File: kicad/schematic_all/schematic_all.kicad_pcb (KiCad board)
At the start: 2 copper layers, 88.9 x 88.9 mm, 36 parts, among them J1 Power In, SW1 Button 1, SW2 Encoder 1, SW3 Button 2, SW4 Encoder 2, SW5 Button 3, U2 RPi_Pico, U3 RDA5807M_Module, U4 LM386

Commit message: schematic v0.2
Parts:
- removed C1, C2, C3: 100uF, Capacitor_THT:CP_Radial_D5.0mm_P2.00mm
- removed C11: 10uF, Capacitor_THT:CP_Radial_D5.0mm_P2.00mm
- removed C7: 220nF, Capacitor_THT:CP_Radial_D5.0mm_P2.00mm
- removed C8: 47pF, Capacitor_THT:C_Rect_L7.0mm_W2.5mm_P5.00mm
- removed C9: 22uF, Capacitor_THT:CP_Radial_D5.0mm_P2.00mm
- moved J1 63.0 mm to (125.8, 120.7), turned to 0 degrees
- moved C4 22.5 mm to (64.2, 110.5), turned to 180 degrees
- moved U4 16.2 mm to (108.0, 102.3)
- moved R3 15.5 mm to (69.8, 116.8), turned to 90 degrees
- moved RV1 13.2 mm to (131.4, 56.6)
- moved RV2 13.1 mm to (131.4, 71.8)
- moved C13 12.0 mm to (127.0, 96.5)
- moved R4 11.5 mm to (119.4, 69.8), turned to -90 degrees
- moved LS1 9.60 mm to (139.1, 110.5)
- moved C5 8.91 mm to (127.0, 71.1), turned to 180 degrees
- moved DISP1 8.89 mm to (89.4, 120.7)
- moved C12 7.20 mm to (128.3, 104.1), turned to -90 degrees
- moved C10 6.82 mm to (120.7, 106.1), turned to 90 degrees
- moved R5 5.75 mm to (129.5, 111.8), turned to 180 degrees
- moved C6 3.12 mm to (127.0, 78.7)
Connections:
- R4 pad 1: Net-(C7-Pad1) -> Net-(U4-+)
- RV1 pad 2: Net-(C7-Pad1) -> Net-(U4-+)
- RV1 pad 3: Net-(C7-Pad1) -> Net-(U4-+)
- RV2 pad 2: Net-(C7-Pad1) -> Net-(U4-+)
- RV2 pad 3: Net-(C7-Pad1) -> Net-(U4-+)
- U4 pad 2: Net-(U4--) -> GND
- U4 pad 7: Net-(U4-BYPASS) -> unconnected-(U4-BYPASS-Pad7)
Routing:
- net /SDC: track 60.8 -> 0.00 mm
- net /SCS: track 53.6 -> 0.00 mm
- net /SRES: track 38.5 -> 0.00 mm
- net /SSDA: track 31.4 -> 0.00 mm
- net /SSCK: track 26.8 -> 0.00 mm
- net /ENC2_CL: track 17.5 -> 0.00 mm
- net /ENC2_DR: track 15.7 -> 0.00 mm
- net /ENC2_PB: track 14.7 -> 0.00 mm
- net Net-(AE1-A): track 0.00 -> 14.2 mm
- net /BTN3: track 13.0 -> 0.00 mm
- net /BTN2: track 12.5 -> 0.00 mm

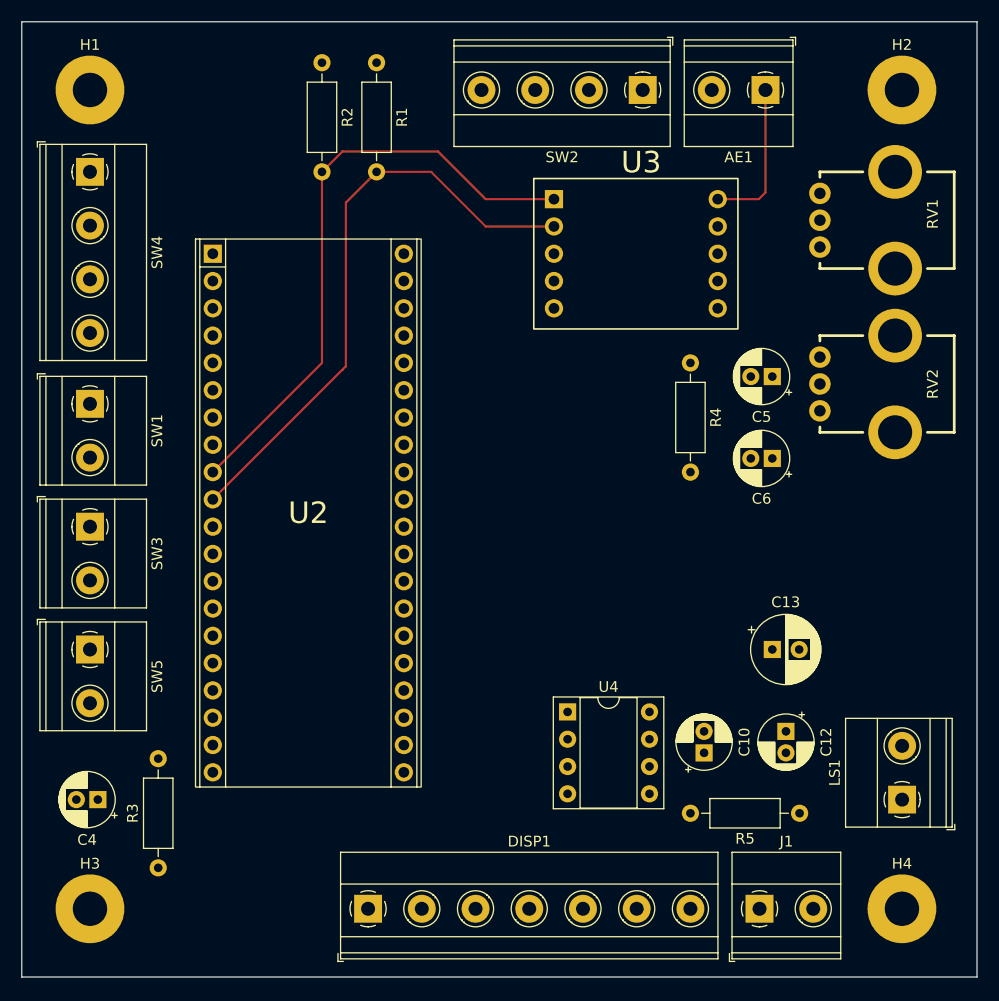
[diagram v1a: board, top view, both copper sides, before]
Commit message: Made some minor changes to the schmatic (Changed PWM pin, filtering capacitor footprints and values), and made some progress on the layout & design of the PCB
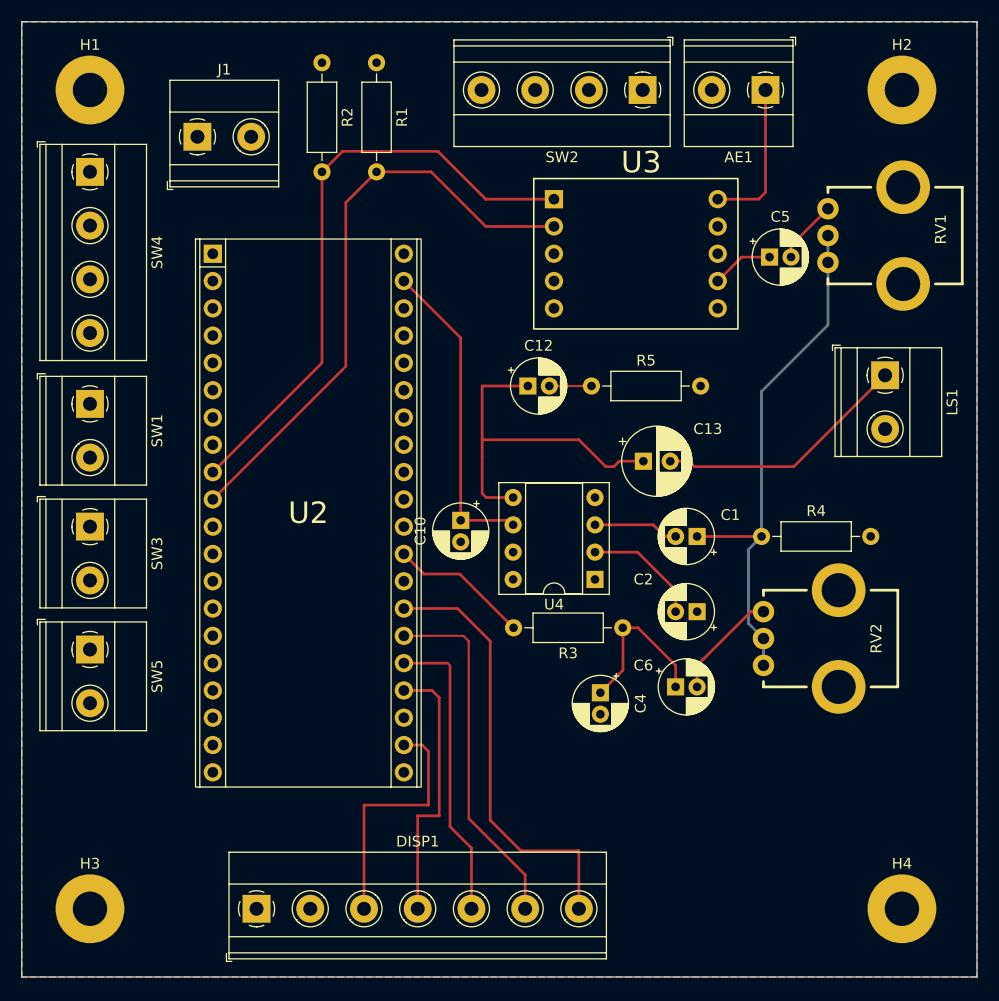
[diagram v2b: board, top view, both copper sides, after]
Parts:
- added C1: 220nF, Capacitor_THT:CP_Radial_D5.0mm_P2.00mm, F.Cu at (120.0, 86.0)
- added C2: 220nF, Capacitor_THT:CP_Radial_D5.0mm_P2.00mm, F.Cu at (120.0, 93.0)
- C4: value 100pF -> 100nF
- moved J1 88.9 mm to (73.5, 48.8)
- moved R3 48.7 mm to (113.1, 94.5), turned to 180 degrees
- moved C4 47.8 mm to (111.0, 100.5), turned to -90 degrees
- moved R5 44.2 mm to (110.2, 72.0), turned to 0 degrees
- moved C12 40.1 mm to (104.2, 72.0), turned to 0 degrees
- moved LS1 39.5 mm to (137.5, 71.0), turned to -90 degrees
- moved C10 31.3 mm to (98.0, 84.5), turned to -90 degrees
- moved RV2 24.3 mm to (126.2, 95.5)
- moved C6 23.1 mm to (118.0, 100.0), turned to 0 degrees
- moved C13 21.2 mm to (115.0, 79.0)
- moved R4 17.5 mm to (126.0, 86.0), turned to 0 degrees
- moved U4 12.6 mm to (110.5, 90.0), turned to 180 degrees
- moved C5 11.1 mm to (126.7, 60.0), turned to 0 degrees
- moved DISP1 10.4 mm to (79.0, 120.7)
- moved RV1 1.61 mm to (132.2, 58.0)
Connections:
- R4 pad 1: Net-(U4-+) -> Net-(C1-Pad1)
- RV1 pad 2: Net-(U4-+) -> Net-(C1-Pad1)
- RV1 pad 3: Net-(U4-+) -> Net-(C1-Pad1)
- RV2 pad 2: Net-(U4-+) -> Net-(C1-Pad1)
- RV2 pad 3: Net-(U4-+) -> Net-(C1-Pad1)
- U2 pad 20: /PWM -> unconnected-(U2-GP15-Pad20)
- U2 pad 29: unconnected-(U2-GP22-Pad29) -> /PWM
- U4 pad 2: GND -> Net-(U4--)
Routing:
- net Net-(C1-Pad1): track 0.00 -> 49.6 mm
- net /SRES: track 0.00 -> 40.8 mm
- net Net-(C12-Pad1): track 0.00 -> 33.9 mm
- net /SDC: track 0.00 -> 33.3 mm
- net +5V: track 0.00 -> 29.5 mm
- net /SSDA: track 0.00 -> 27.9 mm
- net /SSCK: track 0.00 -> 25.2 mm
- net Net-(C13-Pad2): track 0.00 -> 23.7 mm
- net /SCS: track 0.00 -> 23.2 mm
- net Net-(C4-Pad1): track 0.00 -> 15.3 mm
- net /PWM: track 0.00 -> 13.1 mm
- net Net-(U4--): track 0.00 -> 11.0 mm
- net Net-(C6-Pad2): track 0.00 -> 10.2 mm
- net Net-(U4-+): track 0.00 -> 7.95 mm
- net Net-(C5-Pad2): track 0.00 -> 5.92 mm
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- added copper zone on B.Cu, net (none)
- added copper zone on F.Cu, net +3.3V

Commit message: Minor change to Power In placement, and added a corresponding track to VSYS
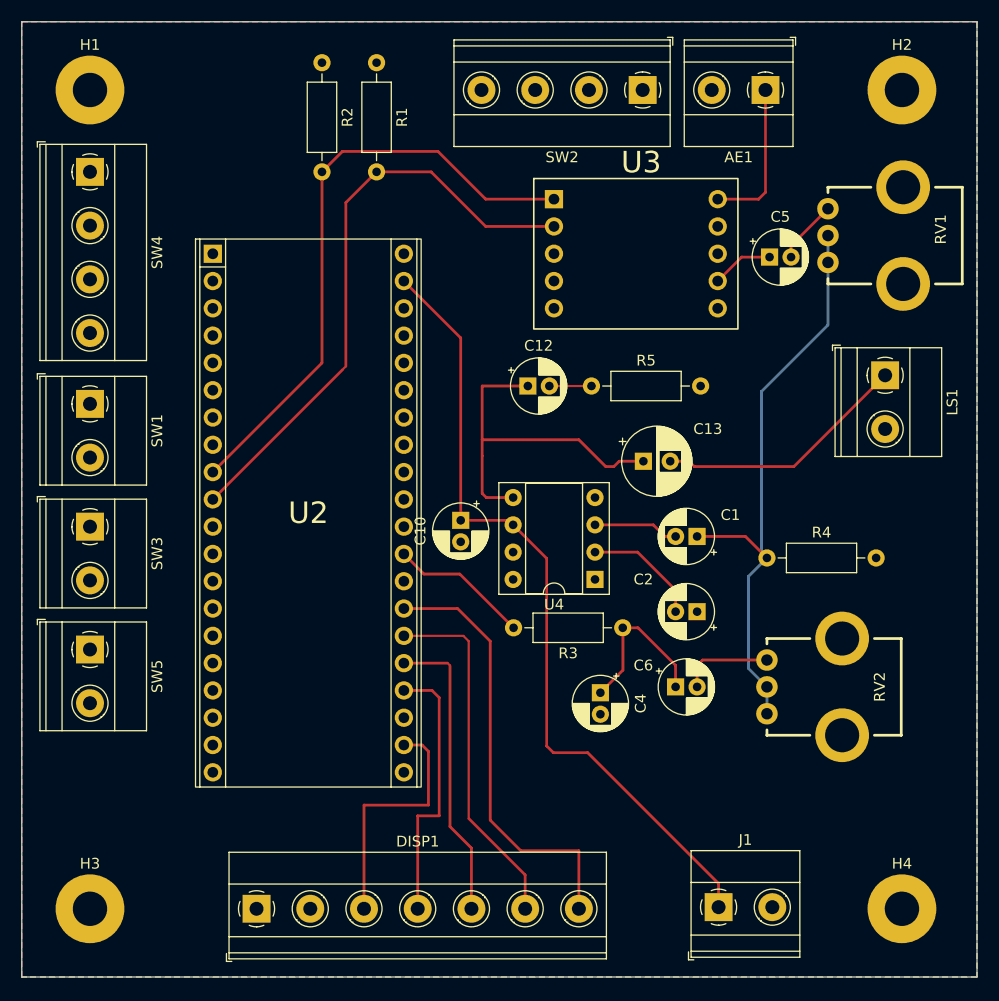
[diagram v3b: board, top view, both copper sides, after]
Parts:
- moved J1 86.6 mm to (122.0, 120.5)
- moved RV2 4.51 mm to (126.5, 100.0)
- moved R4 2.06 mm to (126.5, 88.0)
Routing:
- net +5V: track 29.5 -> 74.9 mm
- net Net-(C1-Pad1): track 49.6 -> 56.0 mm
- net Net-(C6-Pad2): track 10.2 -> 8.71 mm
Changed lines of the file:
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@@
 		(tags "Resistor Axial_DIN0207 series Axial Horizontal pin pitch 10.16mm 0.25W = 1/4W length 6.3mm diameter 2.5mm")
 		(property "Reference" "R5"
-			(at 5.08 -2.37 360)
+			(at 5.08 -2.37 0)
 			(layer "F.SilkS")
 			(effects
@@
 		)
 		(property "Value" "10"
-			(at 5.08 2.37 360)
+			(at 5.08 2.37 0)
 			(layer "F.Fab")
 			(effects
@@
 		)
 		(fp_text user "${REFERENCE}"
-			(at 5.08 0 360)
+			(at 5.08 0 0)
 			(layer "F.Fab")
 			(effects
@@
 		(tags "CP Radial series Radial pin pitch 2.00mm  diameter 5mm Electrolytic Capacitor")
 		(property "Reference" "C5"
-			(at 1 -3.75 360)
+			(at 1 -3.75 0)
 			(layer "F.SilkS")
 			(effects
@@
 		)
 		(property "Value" "100uF"
-			(at 1 3.75 360)
+			(at 1 3.75 0)
 			(layer "F.Fab")
 			(effects
@@
 		)
 		(fp_text user "${REFERENCE}"
-			(at 1 0 360)
+			(at 1 0 0)
 			(layer "F.Fab")
 			(effects
@@
 		(tags "Resistor Axial_DIN0207 series Axial Horizontal pin pitch 10.16mm 0.25W = 1/4W length 6.3mm diameter 2.5mm")
 		(property "Reference" "R3"
-			(at 5.08 -2.37 360)
+			(at 5.08 -2.37 0)
 			(layer "F.SilkS")
 			(effects
@@
 		)
 		(property "Value" "220"
-			(at 5.08 2.37 360)
+			(at 5.08 2.37 0)
 			(layer "F.Fab")
 			(effects
@@
 		)
 		(fp_text user "${REFERENCE}"
-			(at 5.08 0 360)
+			(at 5.08 0 0)
 			(layer "F.Fab")
 			(effects
@@
 		(tags "CP Radial series Radial pin pitch 2.50mm  diameter 6.3mm Electrolytic Capacitor")
 		(property "Reference" "C13"
-			(at 6 -3 360)
+			(at 6 -3 0)
 			(layer "F.SilkS")
 			(effects
@@
 		)
 		(property "Value" "470uF"
-			(at 7 -1 360)
+			(at 7 -1 0)
 			(layer "F.Fab")
 			(effects
@@
 		)
 		(fp_text user "${REFERENCE}"
-			(at 1.25 0 360)
+			(at 1.25 0 0)
 			(layer "F.Fab")
 			(effects
@@
 		(tags "CP Radial series Radial pin pitch 2.00mm  diameter 5mm Electrolytic Capacitor")
 		(property "Reference" "C2"
-			(at 5 3 360)
+			(at 5 3 0)
 			(layer "F.SilkS")
 			(effects
@@
 		)
 		(property "Value" "220nF"
-			(at -4 2 360)
+			(at -4 2 0)
 			(layer "F.Fab")
 			(effects
@@
 		)
 		(fp_text user "${REFERENCE}"
-			(at 1 0 360)
+			(at 1 0 0)
 			(layer "F.Fab")
 			(effects
@@
 	(footprint "TerminalBlock_Phoenix:TerminalBlock_Phoenix_MKDS-1,5-2_1x02_P5.00mm_Horizontal"
 		(layer "F.Cu")
-		(at 73.5 48.805)
+		(at 122 120.5)
 		(descr "Terminal Block Phoenix MKDS-1,5-2, 2 pins, pitch 5mm, size 10x9.8mm^2, drill diamater 1.3mm, pad diameter 2.6mm, see http://www.farnell.com/datasheets/100425.pdf, script-generated using https://github.com/pointhi/kicad-footprint-generator/scripts/TerminalBlock_Phoenix")
 		(tags "THT Terminal Block Phoenix MKDS-1,5-2 pitch 5mm size 10x9.8mm^2 drill 1.3mm pad 2.6mm")
@@
 	(footprint "ECE:Bourns_PTV09_Horiz"
 		(layer "F.Cu")
-		(at 126.1785 95.5 -90)
+		(at 126.5 100 -90)
 		(descr "Pot")
 		(tags "R")
@@
 		(tags "CP Radial series Radial pin pitch 2.00mm  diameter 5mm Electrolytic Capacitor")
 		(property "Reference" "C12"
-			(at 1 -3.75 360)
+			(at 1 -3.75 0)
 			(layer "F.SilkS")
 			(effects
@@
 		)
 		(property "Value" "100nF"
-			(at 1 3.75 360)
+			(at 1 3.75 0)
 			(layer "F.Fab")
 			(effects
@@
 		)
 		(fp_text user "${REFERENCE}"
-			(at 1 0 360)
+			(at 1 0 0)
 			(layer "F.Fab")
 			(effects
@@
 		(tags "CP Radial series Radial pin pitch 2.00mm  diameter 5mm Electrolytic Capacitor")
 		(property "Reference" "C6"
-			(at -3 -2 360)
+			(at -3 -2 0)
 			(layer "F.SilkS")
 			(effects
@@
 		)
 		(property "Value" "100uF"
-			(at 1 3.75 360)
+			(at 1 3.75 0)
 			(layer "F.Fab")
 			(effects
@@
 		)
 		(fp_text user "${REFERENCE}"
-			(at 1 0 360)
+			(at 1 0 0)
 			(layer "F.Fab")
 			(effects
@@
 		(tags "THT DIP DIL PDIP 2.54mm 7.62mm 300mil Socket")
 		(property "Reference" "U4"
-			(at 3.81 -2.33 360)
+			(at 3.81 -2.33 0)
 			(layer "F.SilkS")
 			(effects
@@
 		)
 		(property "Value" "LM386"
-			(at 3.81 9.95 360)
+			(at 3.81 9.95 0)
 			(layer "F.Fab")
 			(effects
@@
 		)
 		(fp_text user "${REFERENCE}"
-			(at 3.8 3.8 360)
+			(at 3.8 3.8 0)
 			(layer "F.Fab")
 			(effects
@@
 	(footprint "Resistor_THT:R_Axial_DIN0207_L6.3mm_D2.5mm_P10.16mm_Horizontal"
 		(layer "F.Cu")
-		(at 126 86)
+		(at 126.5 88)
 		(descr "Resistor, Axial_DIN0207 series, Axial, Horizontal, pin pitch=10.16mm, 0.25W = 1/4W, length*diameter=6.3*2.5mm^2, http://cdn-reichelt.de/documents/datenblatt/B400/1_4W%23YAG.pdf")
 		(tags "Resistor Axial_DIN0207 series Axial Horizontal pin pitch 10.16mm 0.25W = 1/4W length 6.3mm diameter 2.5mm")
 		(property "Reference" "R4"
-			(at 5.08 -2.37 360)
+			(at 5.08 -2.37 0)
 			(layer "F.SilkS")
 			(effects
@@
 		)
 		(property "Value" "2k2"
-			(at 5.08 2.37 360)
+			(at 5.08 2.37 0)
 			(layer "F.Fab")
 			(effects
@@
 		)
 		(fp_text user "${REFERENCE}"
-			(at 5.08 0 360)
+			(at 5.08 0 0)
 			(layer "F.Fab")
 			(effects
@@
 		(tags "CP Radial series Radial pin pitch 2.00mm  diameter 5mm Electrolytic Capacitor")
 		(property "Reference" "C1"
-			(at -3.1 2 360)
+			(at -3.1 2 0)
 			(layer "F.SilkS")
 			(effects
@@
 		)
 		(property "Value" "220nF"
-			(at -4.5 0 360)
+			(at -4.5 0 0)
 			(layer "F.Fab")
 			(effects
@@
 		)
 		(fp_text user "${REFERENCE}"
-			(at 1 0 360)
+			(at 1 0 0)
 			(layer "F.Fab")
 			(effects
@@
 	)
 	(segment
+		(start 106 88.04)
+		(end 102.88 84.92)
+		(width 0.254)
+		(layer "F.Cu")
+		(net 3)
+	)
+	(segment
+		(start 122 118.305)
+		(end 109.819 106.124)
+		(width 0.254)
+		(layer "F.Cu")
+		(net 3)
+	)
+	(segment
 		(start 98 67.52)
 		(end 98 84.5)
@@
 	)
 	(segment
+		(start 122 120.5)
+		(end 122 118.305)
+		(width 0.254)
+		(layer "F.Cu")
+		(net 3)
+	)
+	(segment
+		(start 109.819 106.124)
+		(end 106.624 106.124)
+		(width 0.254)
+		(layer "F.Cu")
+		(net 3)
+	)
+	(segment
 		(start 92.71 62.23)
 		(end 98 67.52)
@@
 	)
 	(segment
+		(start 106 105.5)
+		(end 106 88.04)
+		(width 0.254)
+		(layer "F.Cu")
+		(net 3)
+	)
+	(segment
+		(start 106.624 106.124)
+		(end 106 105.5)
+		(width 0.254)
+		(layer "F.Cu")
+		(net 3)
+	)
+	(segment
 		(start 102.46 84.5)
 		(end 102.88 84.92)
@@
 	)
 	(segment
-		(start 120 100)
-		(end 120 98)
+		(start 120.5 97.5)
+		(end 126.5 97.5)
 		(width 0.254)
 		(layer "F.Cu")
@@
 	)
 	(segment
-		(start 125 93)
-		(end 126.1785 93)
+		(start 120 100)
+		(end 120 98)
 		(width 0.254)
 		(layer "F.Cu")
@@
 	(segment
 		(start 120 98)
-		(end 125 93)
+		(end 120.5 97.5)
 		(width 0.254)
 		(layer "F.Cu")
@@
 	)
 	(segment
-		(start 126 86)
+		(start 124.5 86)
 		(end 120 86)
 		(width 0.254)
@@
 	)
 	(segment
+		(start 126.5 88)
+		(end 124.5 86)
+		(width 0.254)
+		(layer "F.Cu")
+		(net 49)
+	)
+	(segment
 		(start 132.1785 66.3215)
 		(end 126 72.5)
@@
 	)
 	(segment
-		(start 124.7975 87.2025)
-		(end 126 86)
+		(start 132.1785 60.5)
+		(end 132.1785 66.3215)
 		(width 0.254)
 		(layer "B.Cu")
@@
 	)
 	(segment
-		(start 126.1785 98)
-		(end 126.1785 95.5)
+		(start 126.5 102.5)
+		(end 126.5 100)
 		(width 0.254)
 		(layer "B.Cu")
@@
 	)
 	(segment
-		(start 132.1785 60.5)
-		(end 132.1785 58)
+		(start 126 87.5)
+		(end 126.5 88)
 		(width 0.254)
 		(layer "B.Cu")
@@
 	)
 	(segment
-		(start 132.1785 60.5)
-		(end 132.1785 66.3215)
+		(start 124.7975 98.2975)
+		(end 124.7975 89.7025)
 		(width 0.254)
 		(layer "B.Cu")
@@
 	)
 	(segment
-		(start 124.7975 94.119)
-		(end 124.7975 87.2025)
+		(start 126.5 100)
+		(end 124.7975 98.2975)
+		(width 0.254)
+		(layer "B.Cu")
+		(net 49)
+	)
+	(segment
+		(start 132.1785 60.5)
+		(end 132.1785 58)
 		(width 0.254)
 		(layer "B.Cu")
@@
 	(segment
 		(start 126 72.5)
-		(end 126 86)
+		(end 126 87.5)
 		(width 0.254)
 		(layer "B.Cu")
@@
 	)
 	(segment
-		(start 126.1785 95.5)
-		(end 124.7975 94.119)
+		(start 124.7975 89.7025)
+		(end 126.5 88)
 		(width 0.254)
 		(layer "B.Cu")

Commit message: move uploaded files to correct directory
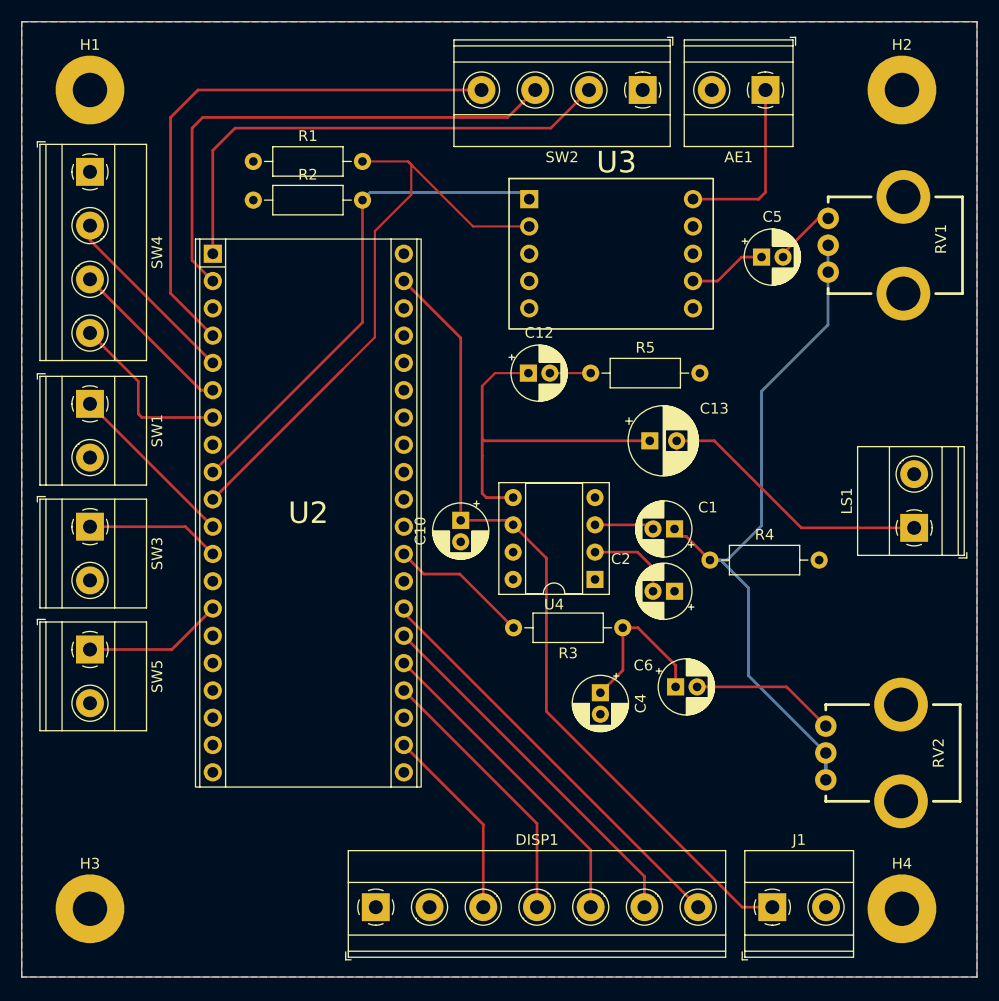
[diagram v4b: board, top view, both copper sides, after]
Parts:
- moved R1 14.7 mm to (78.7, 51.1), turned to 0 degrees
- moved LS1 14.5 mm to (140.2, 85.2), turned to 90 degrees
- moved R2 14.3 mm to (78.7, 54.7), turned to 0 degrees
- moved DISP1 11.1 mm to (90.1, 120.5)
- moved RV2 8.24 mm to (132.0, 106.2)
- moved R4 5.30 mm to (121.2, 88.2)
- moved J1 5.00 mm to (127.0, 120.5)
- moved C2 2.83 mm to (117.9, 91.1)
- moved U3 2.30 mm to (112.0, 59.7)
- moved C1 2.21 mm to (117.9, 85.3)
- moved C13 1.99 mm to (115.6, 77.1)
- moved R5 1.20 mm to (110.1, 70.8)
- moved C12 1.20 mm to (104.3, 70.8)
- moved RV1 0.90 mm to (132.2, 58.9)
- moved C5 0.74 mm to (126.0, 60.0)
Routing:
- net /ENC1_PB: track 0.00 -> 51.9 mm
- net /ENC1_DR: track 0.00 -> 48.4 mm
- net /ENC1_CL: track 0.00 -> 47.0 mm
- net /ENC2_CL: track 0.00 -> 17.5 mm
- net /ENC2_PB: track 0.00 -> 16.5 mm
- net /BTN1: track 0.00 -> 16.2 mm
- net /ENC2_DR: track 0.00 -> 15.7 mm
- net /BTN3: track 0.00 -> 13.0 mm
- net /BTN2: track 0.00 -> 12.5 mm
- net Net-(C1-Pad1): track 56.0 -> 68.2 mm
- net /ISDA: track 56.4 -> 47.1 mm
- net /SCS: track 23.2 -> 18.2 mm
- net Net-(C6-Pad2): track 8.71 -> 13.5 mm
- net Net-(U4--): track 11.0 -> 8.20 mm
- net Net-(U4-+): track 7.95 -> 5.56 mm
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- added copper zone on B.Cu, net GND
- removed copper zone on B.Cu, net (none)
